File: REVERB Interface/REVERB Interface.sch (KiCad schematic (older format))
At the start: 23 parts, among them J1 RPiZeroW, J10 USB, J2 Iridium, J3 APRS, J4 Antenna, J5 MAX3232BOB, J6 USBSER2, J7 USBSER3, J8 USBSER1, J9 USB, M1 MountingHole_Pad, M2 MountingHole_Pad, M3 MountingHole_Pad, M4 MountingHole_Pad, U2 MAX3232, U3 SC16IS752IPW

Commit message: do stuff
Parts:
- removed U3: SC16IS752IPW, Package_SO:TSSOP-28_4.4x9.7mm_P0.65mm, symbol Interface_UART:SC16IS752IPW
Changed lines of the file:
@@
-$EndComp
-$Comp
-L Interface_UART:SC16IS752IPW U3
-U 1 1 615DC7E1
-P 10950 2750
-F 0 "U3" H 10950 3931 50  0000 C CNN
-F 1 "SC16IS752IPW" H 10950 3840 50  0000 C CNN
-F 2 "Package_SO:TSSOP-28_4.4x9.7mm_P0.65mm" H 10950 1200 50  0001 C CNN
-F 3 "https://www.nxp.com/docs/en/data-sheet/SC16IS752_SC16IS762.pdf" H 10950 1350 50  0001 C CNN
-	1    10950 2750
-	1    0    0    -1
 $EndComp
 $Comp

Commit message: bunch of work
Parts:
- removed J6: USBSER2, Connector_PinSocket_2.54mm:PinSocket_1x12_P2.54mm_Vertical, symbol Connector:Conn_01x12_Male
- removed J7: USBSER3, Connector_PinSocket_2.54mm:PinSocket_1x06_P2.54mm_Vertical, symbol Connector:Conn_01x06_Male
- removed J8: USBSER1, Connector_PinSocket_2.54mm:PinSocket_1x12_P2.54mm_Vertical, symbol Connector:Conn_01x12_Male
- removed J9: USB, Connector_PinSocket_2.54mm:PinSocket_1x02_P2.54mm_Vertical, symbol Connector:Conn_01x02_Male
- added C6: 4.7uF, Capacitor_SMD:C_0805_2012Metric_Pad1.18x1.45mm_HandSolder, symbol Device:C
- added C7: 0.1uF, Capacitor_SMD:C_0805_2012Metric_Pad1.18x1.45mm_HandSolder, symbol Device:C
- added C8: 1uF, Capacitor_SMD:C_0805_2012Metric_Pad1.18x1.45mm_HandSolder, symbol Device:C
- added D1, D3, D4, D5: RED, LED_SMD:LED_0805_2012Metric_Pad1.15x1.40mm_HandSolder, symbol Device:LED
- added D2, D6: GREEN, LED_SMD:LED_0805_2012Metric_Pad1.15x1.40mm_HandSolder, symbol Device:LED
- added J6: USB_B_Micro, REVERB Interface:AdafruitMicroB, symbol Connector:USB_B_Micro
- added R1, R2, R3, R4, R5, R6: 1K, Resistor_SMD:R_1206_3216Metric_Pad1.30x1.75mm_HandSolder, symbol Device:R
- added U1: LSM9DS1BOB, REVERB Interface:LSM9DS1BOB, symbol REVERBSym:LSM9DS1BOB
- added U3: CY7C65213-28PVXI, Package_SO:SSOP-28_5.3x10.2mm_P0.65mm, symbol Interface_USB:CY7C65213-28PVXI
- renumbered J10 to J7
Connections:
- net MAX32PWR is gone; now on net SW8: J5.5 (Pin_5)
- net APRSRX: now also D2.1 (K), U3.5 (RXD)
- net APRSTX: now also D1.1 (K), U3.1 (TXD)
- net D+: now also J6.3 (D+), U3.15 (USBDP)
- net D-: now also J6.2 (D-), U3.16 (USBDM)
- net EPSSCL: now also U1.11 (SCL)
- net EPSSDA: now also U1.10 (SDA)
- net GND: now also C6.2, C7.2, C8.2, D3.1 (K), D4.1 (K), J6.5 (GND), J6.6 (Shield), U1.12 (GND), U3.18 (GND), U3.21 (GND), U3.7 (GND)
- net R1OUT: now also D6.1 (K)
- net SW7: now also C6.1, C7.1, J6.1 (VBUS), R1.1, R2.1, R3.1, U3.20 (VCC), U3.4 (VCCIO)
- net SW8: now also R4.1, R5.1, R6.1
- net SW9: now also U1.13 (3V3)
- net T1IN: now also D5.1 (K)
- net SPIMOSI: now reaches J1.19 (12(MOSI))
- net SPIMISO: now reaches J1.21 (13(MISO))
- net SPISCK: now reaches J1.23 (14(SCK))
- net SPICE0: now reaches J1.24 (10(CE0))
- net SPICE1: now reaches J1.26 (11(CE1))
- new net: C8.1, U3.17 (VCCD)
- new net: D1.2 (A), R1.2
- new net: D2.2 (A), R2.2
- new net: D3.2 (A), R3.2
- new net: D4.2 (A), R4.2
- new net: D5.2 (A), R5.2
- new net: D6.2 (A), R6.2
- no-connect marks 67 -> 96
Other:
- note added: "Connectors"
- note added: "IMU"
- note added: "Micro B for programming"
- note added: "UART TO RS232"
- note added: "USB TO UART"
- moved on the sheet: C1, C2, C3, C4, C5, J1, J2, J3, J4, J5, J7, U2

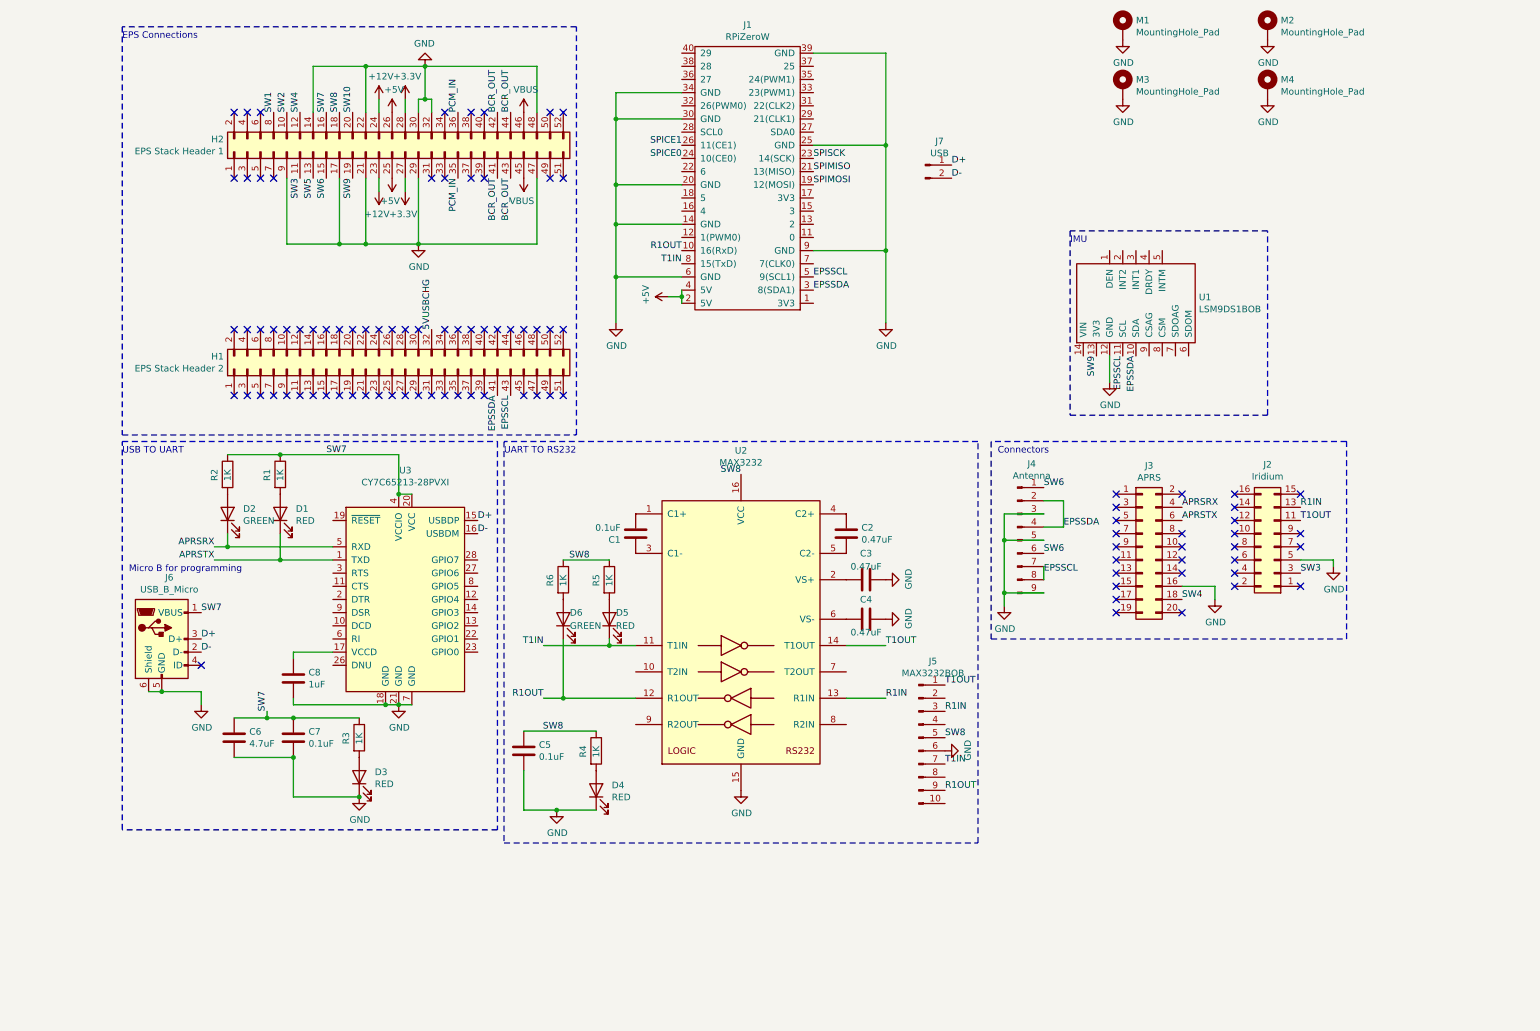
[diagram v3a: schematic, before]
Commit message: add solder jumpers
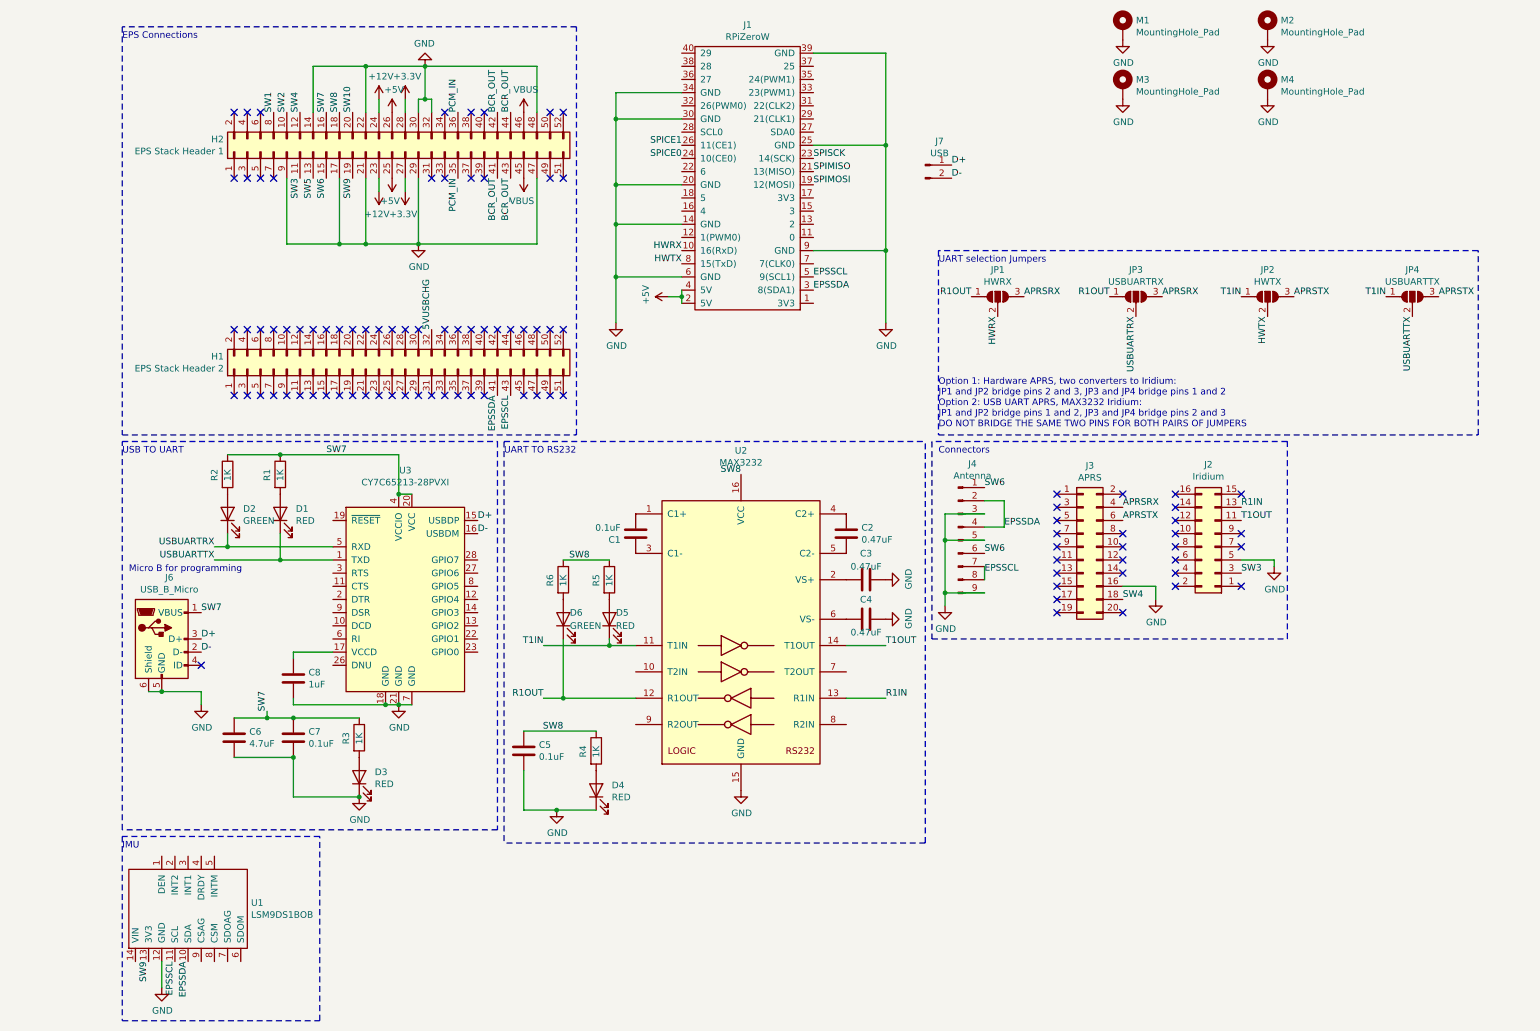
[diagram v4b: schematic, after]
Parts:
- removed J5: MAX3232BOB, Connector_PinSocket_2.54mm:PinSocket_1x10_P2.54mm_Vertical, symbol Connector:Conn_01x10_Male
- added JP1: HWRX, Jumper:SolderJumper-3_P1.3mm_Open_Pad1.0x1.5mm_NumberLabels, symbol Jumper:SolderJumper_3_Open
- added JP2: HWTX, Jumper:SolderJumper-3_P1.3mm_Open_Pad1.0x1.5mm_NumberLabels, symbol Jumper:SolderJumper_3_Open
- added JP3: USBUARTRX, Jumper:SolderJumper-3_P1.3mm_Open_Pad1.0x1.5mm_NumberLabels, symbol Jumper:SolderJumper_3_Open
- added JP4: USBUARTTX, Jumper:SolderJumper-3_P1.3mm_Open_Pad1.0x1.5mm_NumberLabels, symbol Jumper:SolderJumper_3_Open
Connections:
- net APRSRX: now also JP1.3 (B), JP3.3 (B); no longer D2.1 (K), U3.5 (RXD)
- net APRSTX: now also JP2.3 (B), JP4.3 (B); no longer D1.1 (K), U3.1 (TXD)
- net R1OUT: now also JP1.1 (A), JP3.1 (A); no longer J1.10 (16(RxD))
- net T1IN: now also JP2.1 (A), JP4.1 (A); no longer J1.8 (15(TxD))
- new net HWRX: J1.10 (16(RxD)), JP1.2 (C)
- new net HWTX: J1.8 (15(TxD)), JP2.2 (C)
- new net USBUARTRX: D2.1 (K), JP3.2 (C), U3.5 (RXD)
- new net USBUARTTX: D1.1 (K), JP4.2 (C), U3.1 (TXD)
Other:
- note added: "Option 1: Hardware APRS, two converters to Iridium: \nJP1 and JP2 bridge pins 2 and 3, JP3 and JP4 bridge pins 1 and 2\nOption 2: USB UART APRS, MAX3232 Iridium:\nJP1 and JP2 bridge pins 1 and 2, JP3 and JP4 bridge pins 2 and 3\nDO NOT BRIDGE THE SAME TWO PINS FOR BOTH PAIRS OF JUMPERS"
- note added: "UART selection Jumpers"
- moved on the sheet: J2, J3, J4, U1

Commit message: routing work
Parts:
- R1, R2, R3, R4, R5, R6: footprint Resistor_SMD:R_1206_3216Metric_Pad1.30x1.75mm_HandSolder -> Resistor_SMD:R_0805_2012Metric_Pad1.20x1.40mm_HandSolder
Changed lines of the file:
@@
 F 0 "R1" V 1950 4100 50  0000 L CNN
 F 1 "1K" V 2050 4100 50  0000 L CNN
-F 2 "Resistor_SMD:R_1206_3216Metric_Pad1.30x1.75mm_HandSolder" V 1980 4150 50  0001 C CNN
+F 2 "Resistor_SMD:R_0805_2012Metric_Pad1.20x1.40mm_HandSolder" V 1980 4150 50  0001 C CNN
 F 3 "~" H 2050 4150 50  0001 C CNN
 	1    2050 4150
@@
 F 0 "R2" V 1550 4100 50  0000 L CNN
 F 1 "1K" V 1650 4100 50  0000 L CNN
-F 2 "Resistor_SMD:R_1206_3216Metric_Pad1.30x1.75mm_HandSolder" V 1580 4150 50  0001 C CNN
+F 2 "Resistor_SMD:R_0805_2012Metric_Pad1.20x1.40mm_HandSolder" V 1580 4150 50  0001 C CNN
 F 3 "~" H 1650 4150 50  0001 C CNN
 	1    1650 4150
@@
 F 0 "R3" V 2550 6100 50  0000 L CNN
 F 1 "1K" V 2650 6100 50  0000 L CNN
-F 2 "Resistor_SMD:R_1206_3216Metric_Pad1.30x1.75mm_HandSolder" V 2580 6150 50  0001 C CNN
+F 2 "Resistor_SMD:R_0805_2012Metric_Pad1.20x1.40mm_HandSolder" V 2580 6150 50  0001 C CNN
 F 3 "~" H 2650 6150 50  0001 C CNN
 	1    2650 6150
@@
 F 0 "R4" V 4350 6200 50  0000 L CNN
 F 1 "1K" V 4450 6200 50  0000 L CNN
-F 2 "Resistor_SMD:R_1206_3216Metric_Pad1.30x1.75mm_HandSolder" V 4380 6250 50  0001 C CNN
+F 2 "Resistor_SMD:R_0805_2012Metric_Pad1.20x1.40mm_HandSolder" V 4380 6250 50  0001 C CNN
 F 3 "~" H 4450 6250 50  0001 C CNN
 	1    4450 6250
@@
 F 0 "R5" V 4450 4900 50  0000 L CNN
 F 1 "1K" V 4550 4900 50  0000 L CNN
-F 2 "Resistor_SMD:R_1206_3216Metric_Pad1.30x1.75mm_HandSolder" V 4480 4950 50  0001 C CNN
+F 2 "Resistor_SMD:R_0805_2012Metric_Pad1.20x1.40mm_HandSolder" V 4480 4950 50  0001 C CNN
 F 3 "~" H 4550 4950 50  0001 C CNN
 	1    4550 4950
@@
 F 0 "R6" V 4100 4900 50  0000 L CNN
 F 1 "1K" V 4200 4900 50  0000 L CNN
-F 2 "Resistor_SMD:R_1206_3216Metric_Pad1.30x1.75mm_HandSolder" V 4130 4950 50  0001 C CNN
+F 2 "Resistor_SMD:R_0805_2012Metric_Pad1.20x1.40mm_HandSolder" V 4130 4950 50  0001 C CNN
 F 3 "~" H 4200 4950 50  0001 C CNN
 	1    4200 4950
@@
 Wire Notes Line
 	3750 3900 6950 3900
+Entry Wire Line
+	0    6250 100  6350
 $EndSCHEMATC

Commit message: finishing up for real now
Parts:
- added J8: USBPOGO, Connector_PinSocket_2.54mm:PinSocket_1x02_P2.54mm_Vertical, symbol Connector:Conn_01x02_Male
- added M5, M6, M7, M8: PiMount, MountingHole:MountingHole_2.7mm_M2.5, symbol Mechanical:MountingHole
- added TP1: GND, TestPoint:TestPoint_Pad_D2.0mm, symbol Connector:TestPoint
- added TP2: 3V3, TestPoint:TestPoint_Pad_D2.0mm, symbol Connector:TestPoint
- added TP3: 5V, TestPoint:TestPoint_Pad_D2.0mm, symbol Connector:TestPoint
- added TP4: BAT, TestPoint:TestPoint_Pad_D2.0mm, symbol Connector:TestPoint
- added TP5: 12V, TestPoint:TestPoint_Pad_D2.0mm, symbol Connector:TestPoint
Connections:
- net +12V: now also TP5.1
- net +3V3: now also TP2.1
- net +5V: now also TP3.1
- net D+: now also J8.1 (Pin_1)
- net D-: now also J8.2 (Pin_2)
- net GND: now also TP1.1
- net VBUS: now also TP4.1
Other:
- moved on the sheet: M1, M2, M3, M4
